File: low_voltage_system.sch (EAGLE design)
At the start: 14 parts

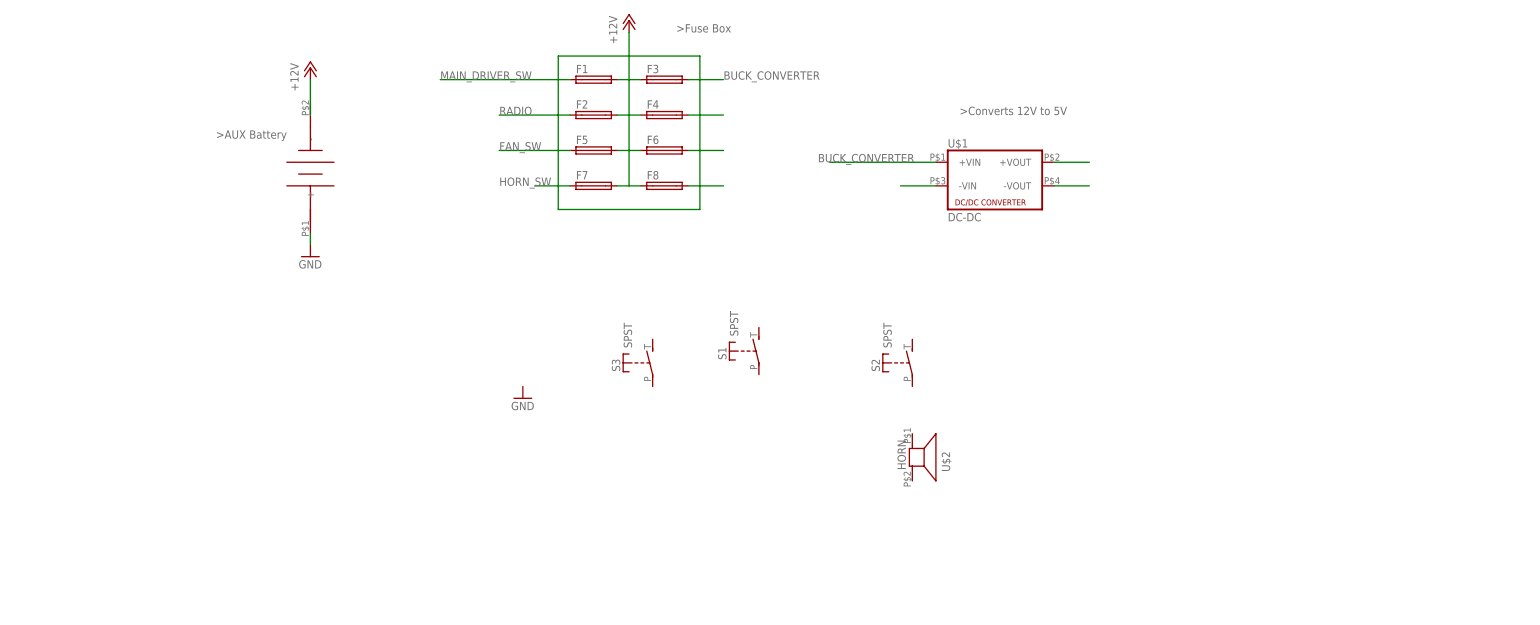
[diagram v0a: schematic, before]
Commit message: added more components to schematic
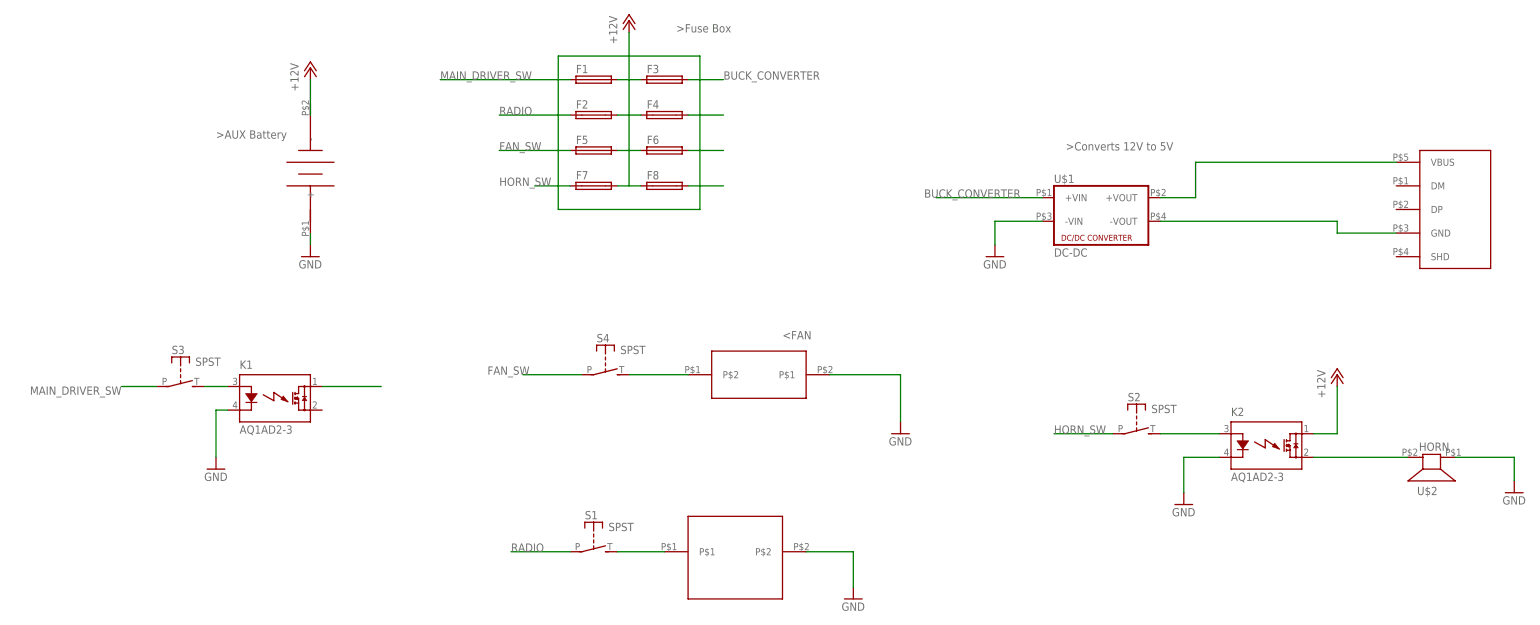
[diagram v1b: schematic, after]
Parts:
- added K1, K2: AQ1AD2-3, relay:AQ1AD2-3
- added S4: SPST, adafruit:SPST
- added U$4: USB_CHARGER, Auxilary:USB_CHARGER
- added U$5: RADIO, Auxilary:RADIO
- added U$6: DRIVER_FAN, Auxilary:DRIVER_FAN
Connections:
- new net N$10: S1.S, U$5.P$1
- new net N$14: K2.A, S2.S
- new net N$15: K2.DS2, U$2.2
- new net N$16: S4.S, U$6.P$2
- new net N$6: K1.A, S3.S
- net +12V: now also K2.DS1
- net FAN_SW: now also S4.P
- net GND: now also K1.K, K2.K, U$1.-VIN, U$2.1, U$5.P$2, U$6.P$1
- net HORN_SW: now also S2.P
- net MAIN_DRIVER_SW: now also S3.P
- net N$7: now also K1.DS1; no longer U$1.-VIN
- net N$8: now also U$4.VBUS
- net N$9: now also U$4.GND
- net RADIO: now also S1.P
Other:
- moved on the sheet: S1, S2, S3, U$1, U$2
